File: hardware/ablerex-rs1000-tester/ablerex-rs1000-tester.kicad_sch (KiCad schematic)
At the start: 29 parts, among them IC1 TMS320F28035PNT, Y1 10MHz

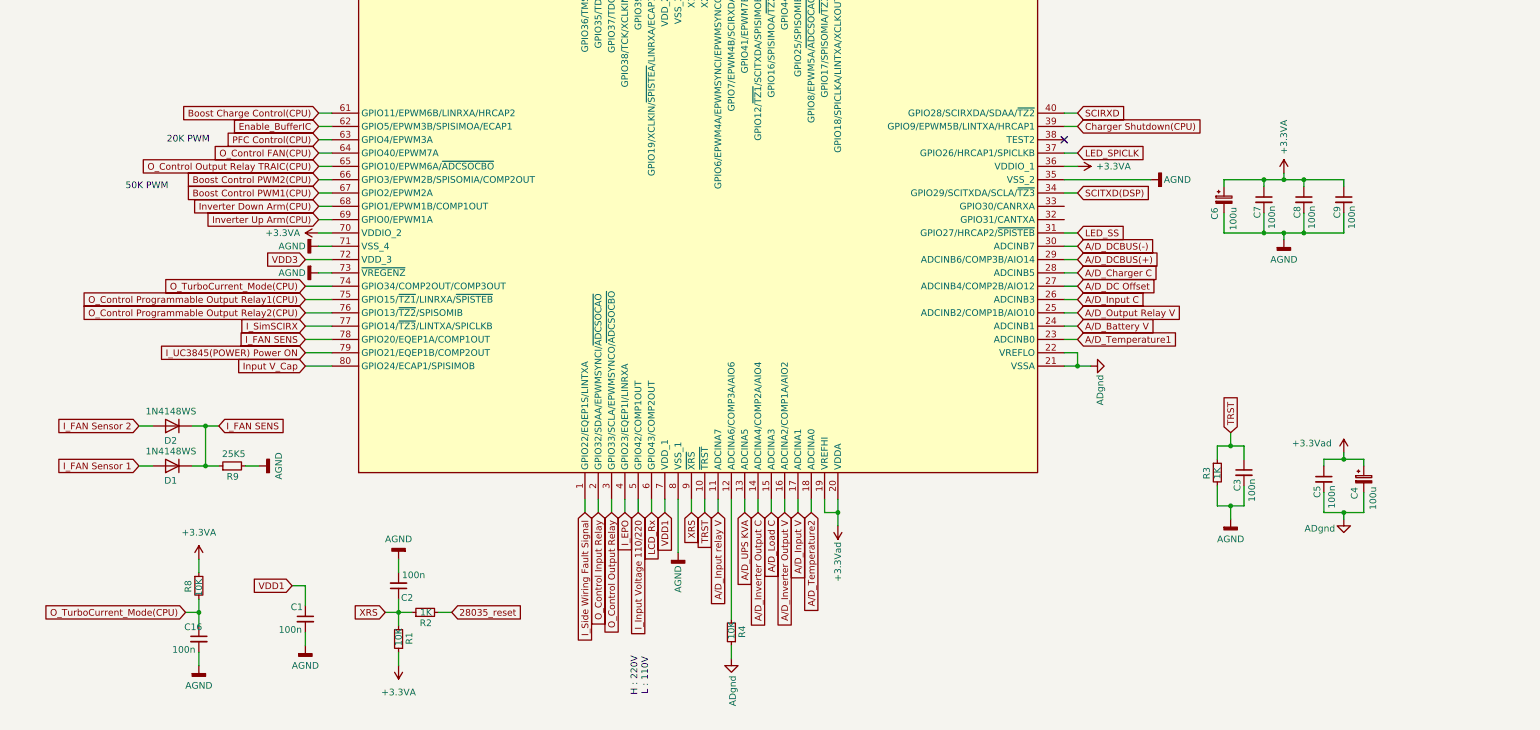
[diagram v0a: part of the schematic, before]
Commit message: Completed the schematic, checked until 40th pin of the MCU
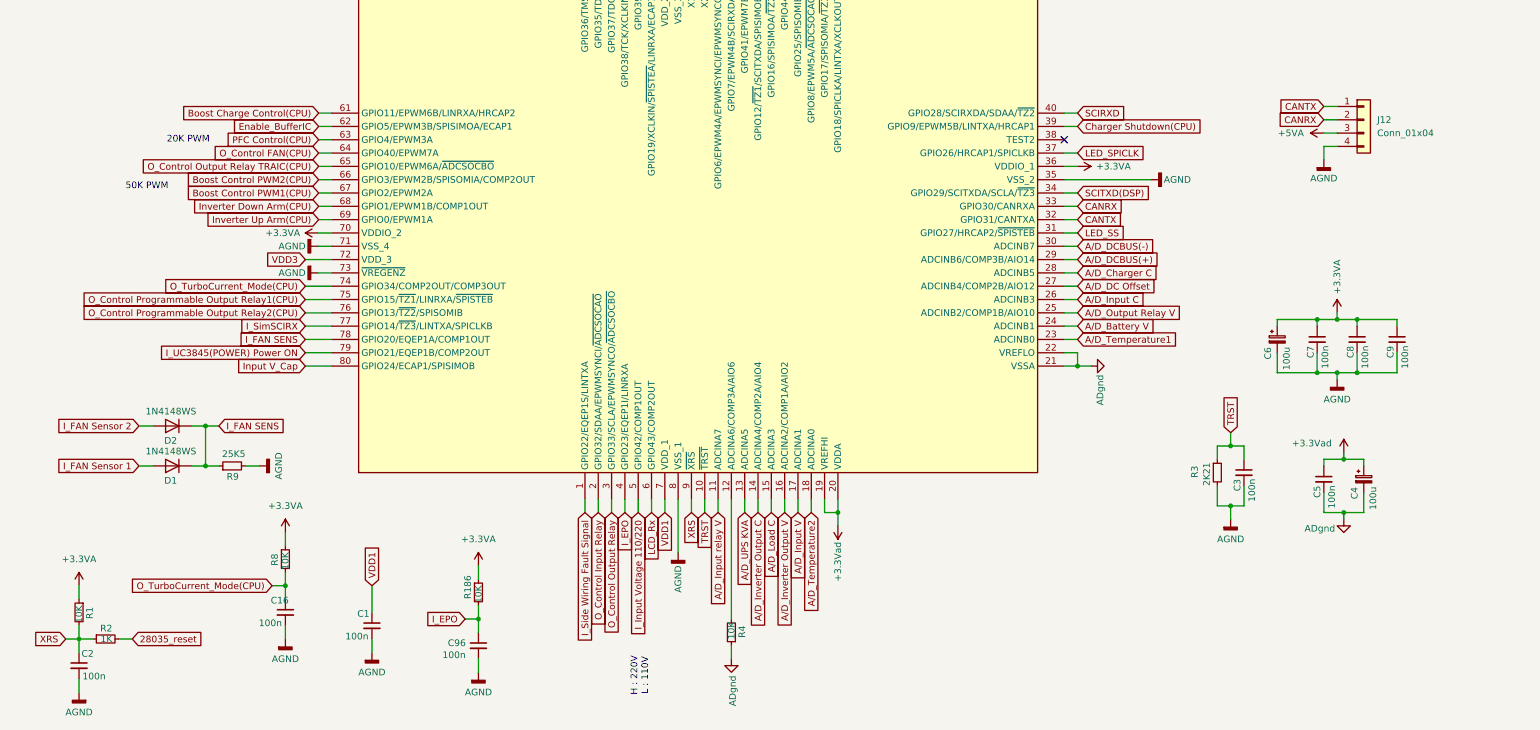
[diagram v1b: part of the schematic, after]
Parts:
- added C96: 100n, symbol Device:C_Small
- added J12: Conn_01x04, symbol Connector_Generic:Conn_01x04
- added R186: 10K, symbol Device:R_Small
- R3: value 1K -> 2K21
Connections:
- net +3.3VA: now also R186.1
- net AGND: now also C96.2, J12.4 (Pin_4)
- net I_EPO: now also C96.1, R186.2
- net CANTX: now reaches IC1.32 (GPIO31/CANTXA)
- net CANTX: now also J12.1 (Pin_1)
- net CANRX: now reaches IC1.33 (GPIO30/CANRXA)
- net CANRX: now also J12.2 (Pin_2)
- new net +5VA: J12.3 (Pin_3)
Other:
- moved on the sheet: C1, C16, C2, C6, C7, C8, C9, R1, R2, R8

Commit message: checked all the schematics
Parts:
- added R187: 10K, symbol Device:R_Small
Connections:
- net +3.3VA: now also R187.1
- net TDO: now also R187.2
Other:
- moved on the sheet: C12, C13, J12, R7, Y1
